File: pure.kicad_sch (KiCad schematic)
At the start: 0 parts

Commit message: schematics mixer progress, 74HC4053, IF RX. PCB update
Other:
- added sheet 74HC4053 (74HC4053.kicad_sch)
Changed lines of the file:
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@@
+		)
+	)
+	(sheet
+		(at 76.835 151.765)
+		(size 41.91 22.86)
+		(fields_autoplaced yes)
+		(stroke
+			(width 0.1524)
+			(type solid)
+		)
+		(fill
+			(color 0 0 0 0.0000)
+		)
+		(property "Sheetname" "74HC4053"
+			(at 76.835 151.0534 0)
+			(effects
+				(font
+					(size 1.27 1.27)
+				)
+				(justify left bottom)
+			)
+		)
+		(property "Sheetfile" "74HC4053.kicad_sch"
+			(at 76.835 175.2096 0)
+			(effects
+				(font
+					(size 1.27 1.27)
+				)
+				(justify left top)
+			)
+		)
+		(instances
+			(project "pure"
+				(path "/74d736cc-15c3-4dc5-ae3c-dc08a689d728"
+					(page "10")
+				)
+			)
 		)
 	)

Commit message: finich IF_RX_Schematics, begin MCU, delete *.sch files
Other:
- sheet IF(RX) renamed IF_RX
- removed sheet VFO
- added sheet MCU (MCU.kicad_sch)
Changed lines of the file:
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@@
 			(color 0 0 0 0.0000)
 		)
-		(property "Sheetname" "IF(RX)"
+		(property "Sheetname" "IF_RX"
 			(at 78.74 58.8514 0)
 			(effects
@@
 	)
 	(sheet
-		(at 20.32 137.16)
-		(size 33.02 15.24)
-		(fields_autoplaced yes)
-		(stroke
-			(width 0)
-			(type solid)
-		)
-		(fill
-			(color 0 0 0 0.0000)
-		)
-		(property "Sheetname" "VFO"
-			(at 20.32 136.3214 0)
-			(effects
-				(font
-					(size 1.524 1.524)
-				)
-				(justify left bottom)
-			)
-		)
-		(property "Sheetfile" "VFO.kicad_sch"
-			(at 20.32 153.0862 0)
-			(effects
-				(font
-					(size 1.524 1.524)
-				)
-				(justify left top)
-			)
-		)
-		(instances
-			(project "pure"
-				(path "/74d736cc-15c3-4dc5-ae3c-dc08a689d728"
-					(page "4")
-				)
-			)
-		)
-	)
-	(sheet
 		(at 193.04 59.69)
 		(size 50.8 31.75)
@@
 				)
 			)
+		)
+	)
+	(sheet
+		(at 25.4 147.574)
+		(size 34.544 24.892)
+		(fields_autoplaced yes)
+		(stroke
+			(width 0.1524)
+			(type solid)
+		)
+		(fill
+			(color 0 0 0 0.0000)
+		)
+		(property "Sheetname" "MCU"
+			(at 25.4 146.8624 0)
+			(effects
+				(font
+					(size 1.27 1.27)
+				)
+				(justify left bottom)
+			)
+		)
+		(property "Sheetfile" "MCU.kicad_sch"
+			(at 25.4 173.0506 0)
+			(effects
+				(font
+					(size 1.27 1.27)
+				)
+				(justify left top)
+			)
+		)
+		(instances
+			(project "pure"
+				(path "/74d736cc-15c3-4dc5-ae3c-dc08a689d728"
+					(page "10")
+				)
+			)

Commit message: schematics mixer progress, mcu
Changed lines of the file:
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@@
 	)
 	(sheet
-		(at 76.835 151.765)
+		(at 79.375 146.431)
 		(size 41.91 22.86)
 		(fields_autoplaced yes)
@@
 		)
 		(property "Sheetname" "74HC4053"
-			(at 76.835 151.0534 0)
+			(at 79.375 145.7194 0)
 			(effects
 				(font
@@
 		)
 		(property "Sheetfile" "74HC4053.kicad_sch"
-			(at 76.835 175.2096 0)
+			(at 79.375 169.8756 0)
 			(effects
 				(font

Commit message: add BPF, add Firmware
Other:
- removed sheet MAX232
- added sheet BPF (BPF.kicad_sch)
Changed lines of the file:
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@@
-	)
-	(sheet
-		(at 137.16 97.79)
-		(size 50.8 31.75)
-		(fields_autoplaced yes)
-		(stroke
-			(width 0)
-			(type solid)
-		)
-		(fill
-			(color 0 0 0 0.0000)
-		)
-		(property "Sheetname" "MAX232"
-			(at 137.16 96.9514 0)
-			(effects
-				(font
-					(size 1.524 1.524)
-				)
-				(justify left bottom)
-			)
-		)
-		(property "Sheetfile" "MAX232.kicad_sch"
-			(at 137.16 130.2262 0)
-			(effects
-				(font
-					(size 1.524 1.524)
-				)
-				(justify left top)
-			)
-		)
-		(instances
-			(project "pure"
-				(path "/74d736cc-15c3-4dc5-ae3c-dc08a689d728"
-					(page "8")
-				)
-			)
-		)
 	)
 	(sheet
@@
 			(effects
 				(font
+					(size 1.27 1.27)
+				)
+				(justify left top)
+			)
+		)
+		(instances
+			(project "pure"
+				(path "/74d736cc-15c3-4dc5-ae3c-dc08a689d728"
+					(page "10")
+				)
+			)
+		)
+	)
+	(sheet
+		(at 137.16 97.79)
+		(size 50.546 31.75)
+		(fields_autoplaced yes)
+		(stroke
+			(width 0.1524)
+			(type solid)
+		)
+		(fill
+			(color 0 0 0 0.0000)
+		)
+		(property "Sheetname" "BPF"
+			(at 137.16 97.0784 0)
+			(effects
+				(font
+					(size 1.27 1.27)
+				)
+				(justify left bottom)
+			)
+		)
+		(property "Sheetfile" "BPF.kicad_sch"
+			(at 137.16 130.1246 0)
+			(effects
+				(font

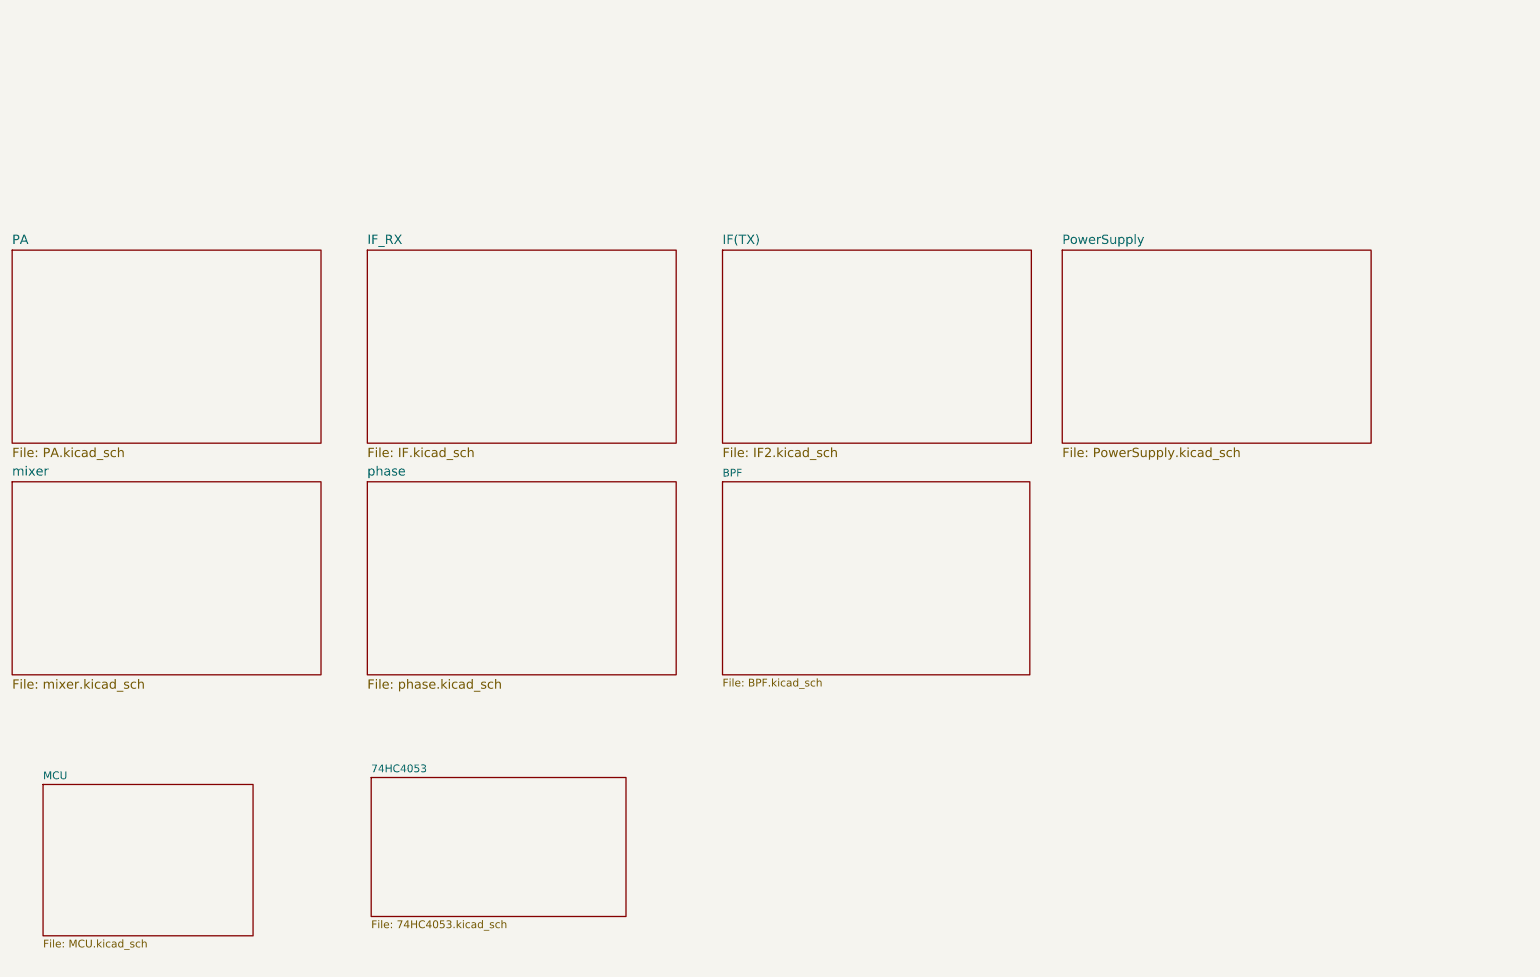
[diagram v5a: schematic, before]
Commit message: progress in PCB, schematics some footprints are still missing
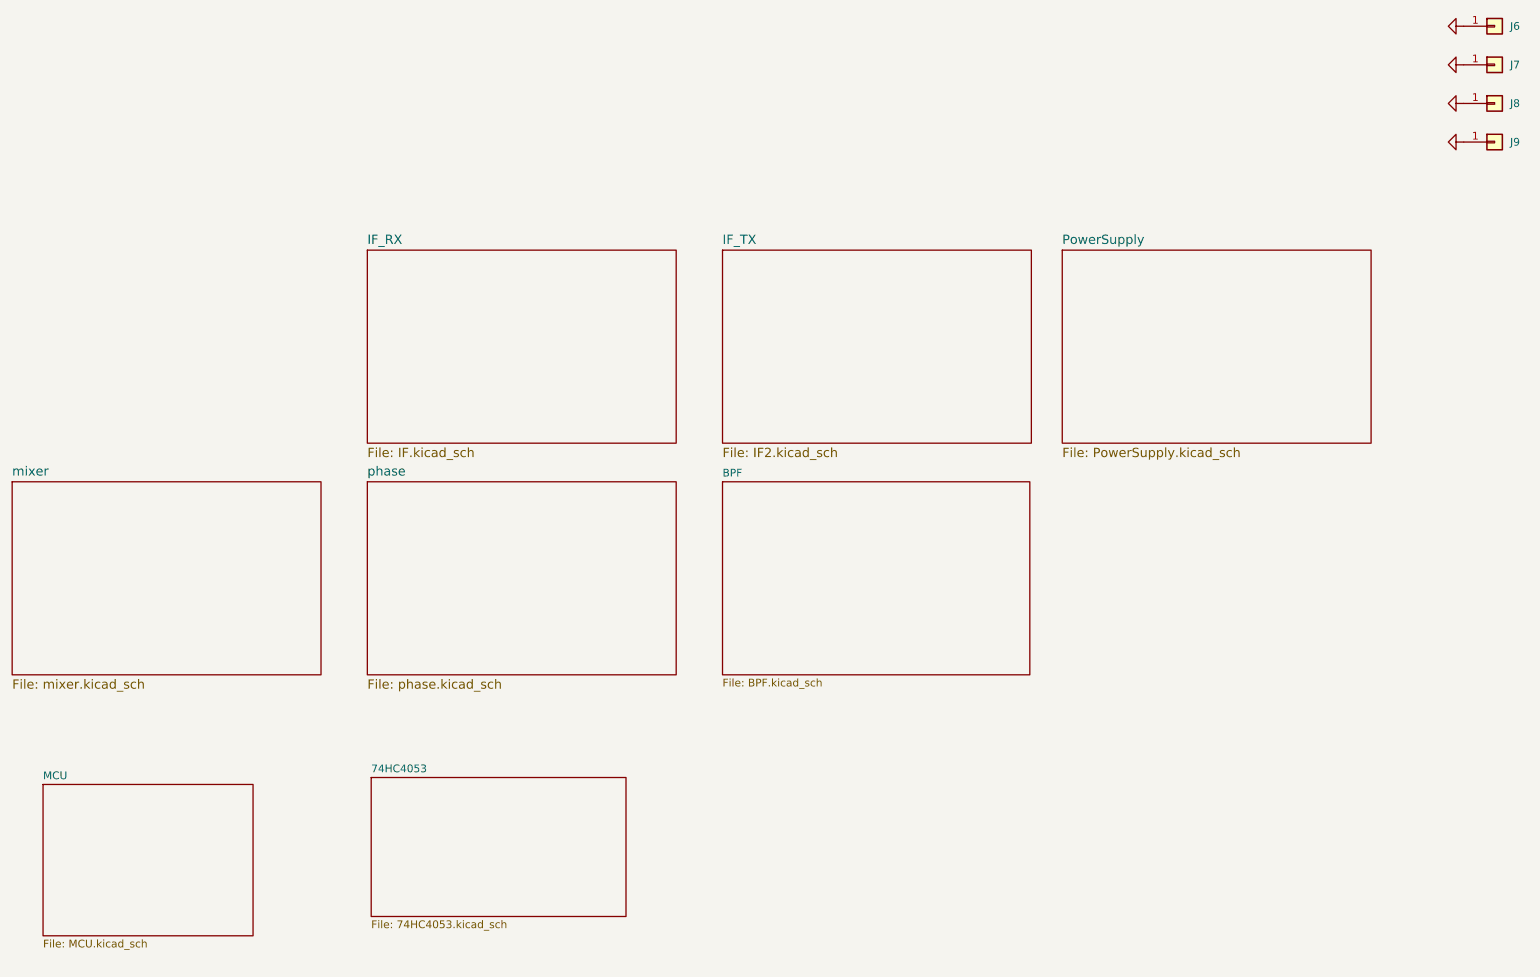
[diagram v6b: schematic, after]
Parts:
- added J6, J7, J8, J9: Conn_01x01, MountingHole:MountingHole_3.2mm_M3_DIN965_Pad, symbol Connector_Generic:Conn_01x01
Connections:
- new net GND: J6.1 (Pin_1), J7.1 (Pin_1), J8.1 (Pin_1), J9.1 (Pin_1)
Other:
- sheet IF(TX) renamed IF_TX
- removed sheet PA
